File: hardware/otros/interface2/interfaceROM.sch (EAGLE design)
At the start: 15 parts, among them IC1 74HC174N, IC2 74HC32N, IC4 AM29F040S

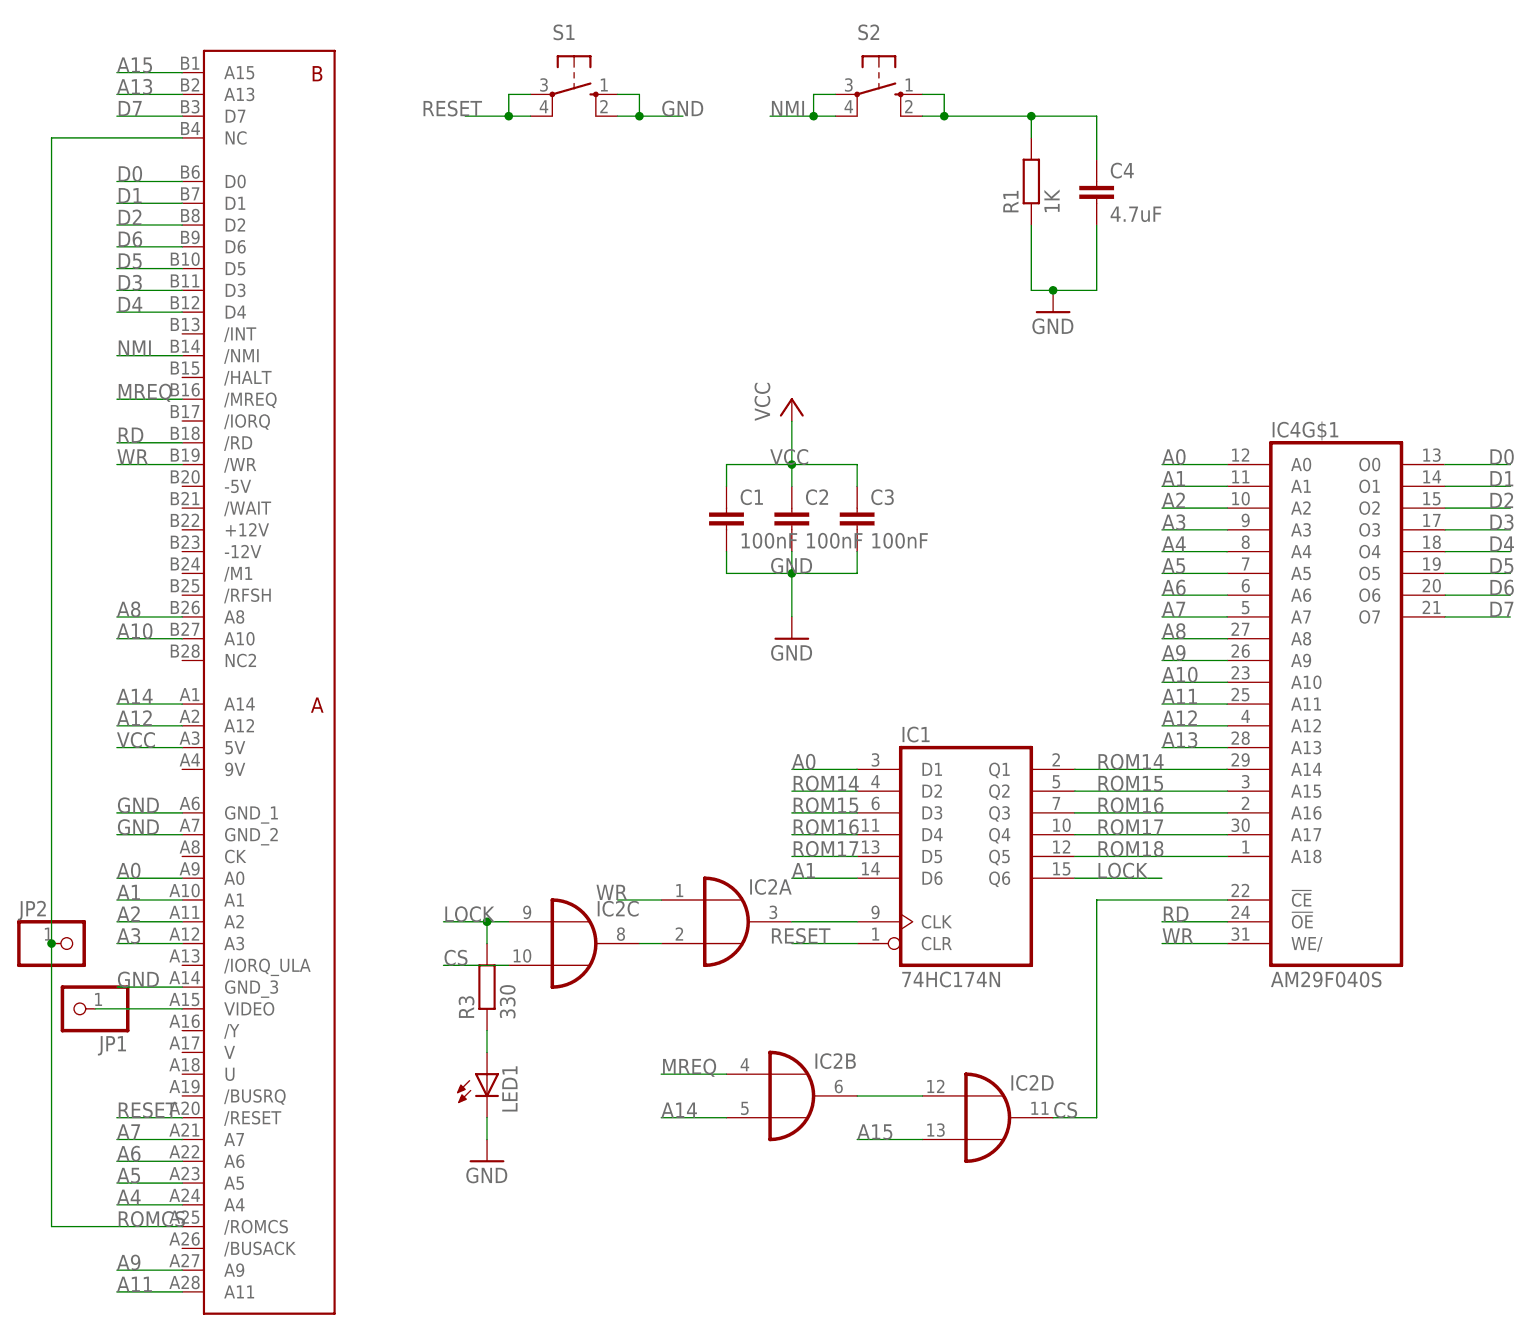
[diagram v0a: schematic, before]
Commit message: 
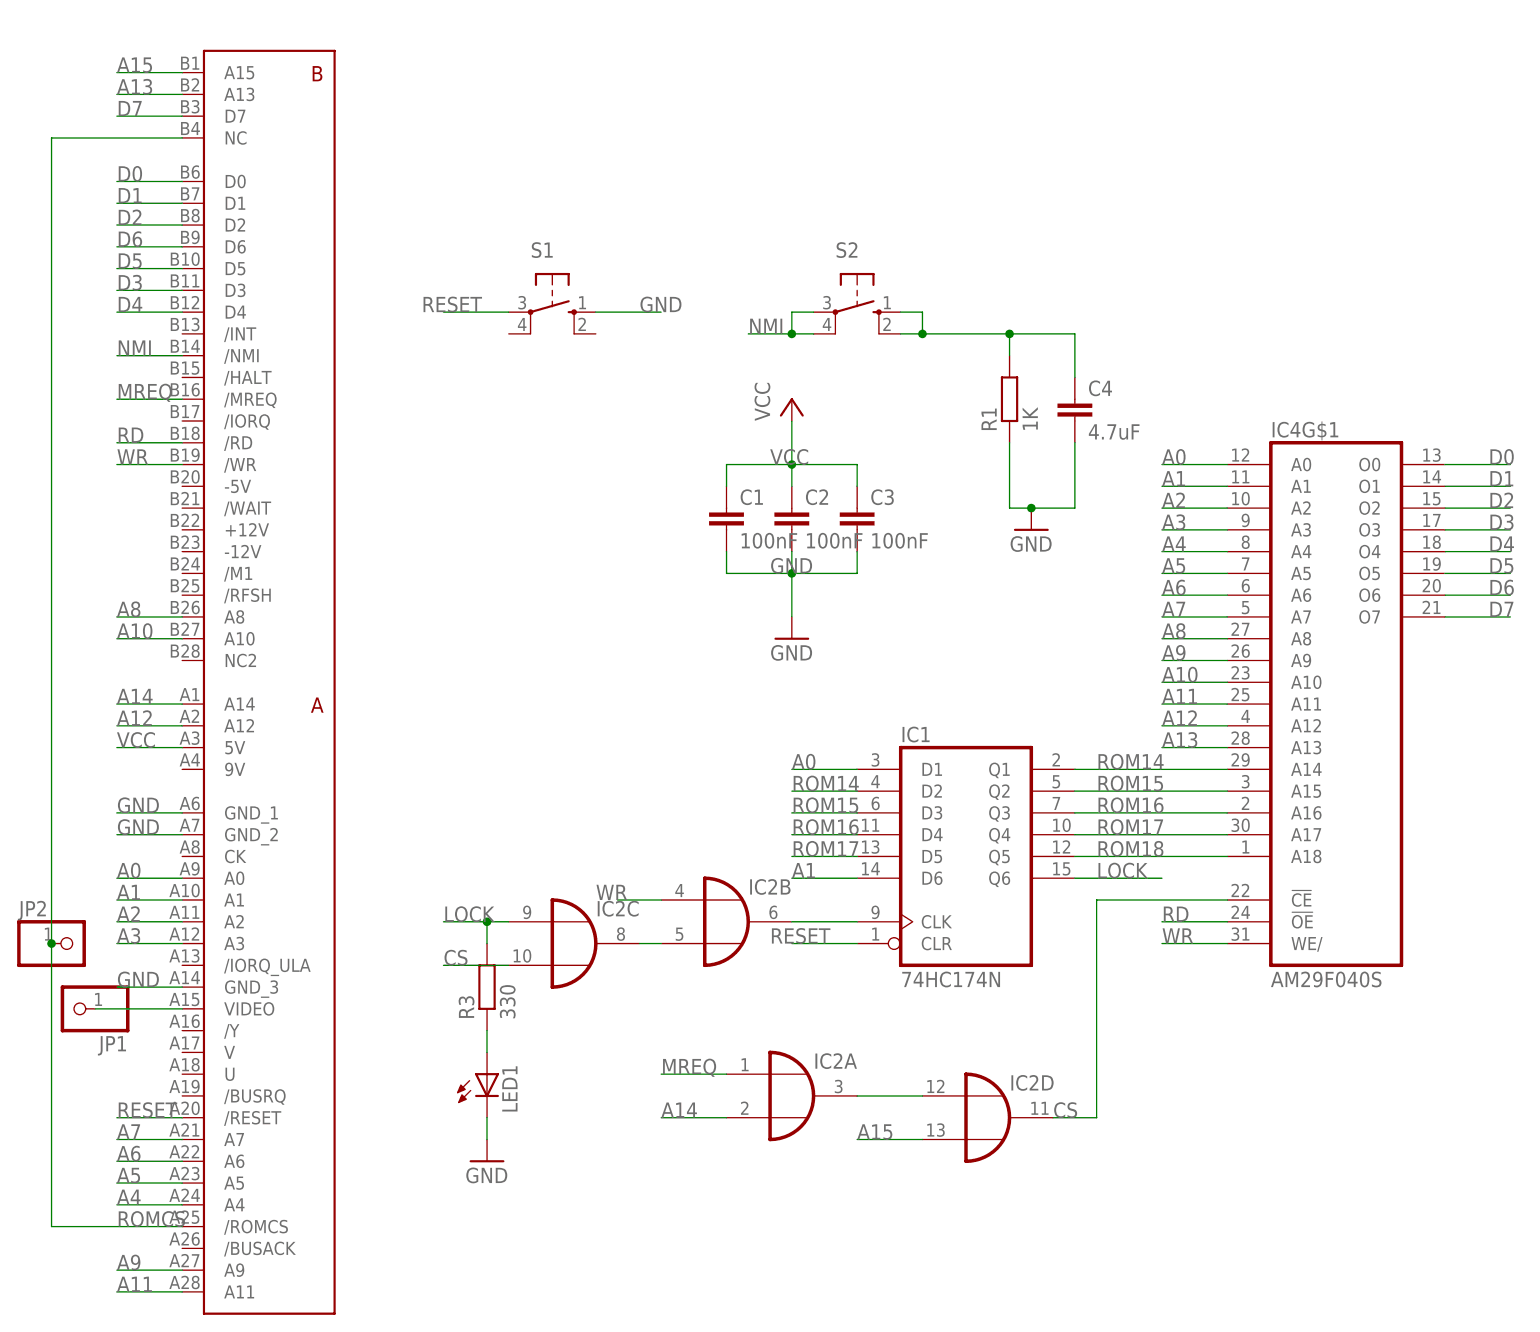
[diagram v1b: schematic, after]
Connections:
- net A14: now also IC2A.I1; no longer IC2B.I1
- net GND: no longer S1.S1
- net MREQ: now also IC2A.I0; no longer IC2B.I0
- net N$2: now also IC2B.O; no longer IC2A.O
- net N$3: now also IC2A.O; no longer IC2B.O
- net N$4: now also IC2B.I1; no longer IC2A.I1
- net RESET: no longer S1.P1
- net WR: now also IC2B.I0; no longer IC2A.I0
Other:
- moved on the sheet: C4, IC2A, IC2B, R1, S1, S2
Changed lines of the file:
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@@
 </plain>
 <instances>
-<instance part="S1" gate="1" x="48.26" y="78.74" rot="R270"/>
-<instance part="S2" gate="1" x="83.82" y="78.74" rot="R270"/>
+<instance part="S1" gate="1" x="45.72" y="53.34" rot="R270"/>
+<instance part="S2" gate="1" x="81.28" y="53.34" rot="R270"/>
 <instance part="U$3" gate="G$1" x="5.08" y="-63.5"/>
-<instance part="R1" gate="G$1" x="101.6" y="68.58" rot="R90"/>
-<instance part="C4" gate="G$1" x="109.22" y="68.58"/>
-<instance part="GND1" gate="1" x="104.14" y="53.34"/>
+<instance part="R1" gate="G$1" x="99.06" y="43.18" rot="R90"/>
+<instance part="C4" gate="G$1" x="106.68" y="43.18"/>
+<instance part="GND1" gate="1" x="101.6" y="27.94"/>
 <instance part="JP2" gate="G$1" x="-10.16" y="-20.32"/>
 <instance part="JP1" gate="G$1" x="-10.16" y="-27.94" rot="R180"/>
@@
 <instance part="C2" gate="G$1" x="73.66" y="30.48"/>
 <instance part="IC2" gate="C" x="48.26" y="-20.32"/>
-<instance part="IC2" gate="A" x="66.04" y="-17.78"/>
-<instance part="IC2" gate="B" x="73.66" y="-38.1"/>
+<instance part="IC2" gate="B" x="66.04" y="-17.78"/>
+<instance part="IC2" gate="A" x="73.66" y="-38.1"/>
 <instance part="IC2" gate="D" x="96.52" y="-40.64"/>
 </instances>
@@
 <segment>
 <pinref part="S2" gate="1" pin="S1"/>
-<wire x1="88.9" y1="76.2" x2="91.44" y2="76.2" width="0.1524" layer="91"/>
+<wire x1="86.36" y1="50.8" x2="88.9" y2="50.8" width="0.1524" layer="91"/>
 <pinref part="S2" gate="1" pin="S"/>
-<wire x1="88.9" y1="78.74" x2="91.44" y2="78.74" width="0.1524" layer="91"/>
-<wire x1="91.44" y1="78.74" x2="91.44" y2="76.2" width="0.1524" layer="91"/>
-<junction x="91.44" y="76.2"/>
+<wire x1="86.36" y1="53.34" x2="88.9" y2="53.34" width="0.1524" layer="91"/>
+<wire x1="88.9" y1="53.34" x2="88.9" y2="50.8" width="0.1524" layer="91"/>
+<junction x="88.9" y="50.8"/>
 <pinref part="C4" gate="G$1" pin="1"/>
-<wire x1="91.44" y1="76.2" x2="101.6" y2="76.2" width="0.1524" layer="91"/>
-<wire x1="101.6" y1="76.2" x2="109.22" y2="76.2" width="0.1524" layer="91"/>
-<wire x1="109.22" y1="76.2" x2="109.22" y2="71.12" width="0.1524" layer="91"/>
+<wire x1="88.9" y1="50.8" x2="99.06" y2="50.8" width="0.1524" layer="91"/>
+<wire x1="99.06" y1="50.8" x2="106.68" y2="50.8" width="0.1524" layer="91"/>
+<wire x1="106.68" y1="50.8" x2="106.68" y2="45.72" width="0.1524" layer="91"/>
 <pinref part="R1" gate="G$1" pin="2"/>
-<wire x1="101.6" y1="73.66" x2="101.6" y2="76.2" width="0.1524" layer="91"/>
-<junction x="101.6" y="76.2"/>
+<wire x1="99.06" y1="48.26" x2="99.06" y2="50.8" width="0.1524" layer="91"/>
+<junction x="99.06" y="50.8"/>
 </segment>
 </net>
@@
 <wire x1="58.42" y1="-40.64" x2="66.04" y2="-40.64" width="0.1524" layer="91"/>
 <label x="58.42" y="-40.64" size="1.778" layer="95"/>
-<pinref part="IC2" gate="B" pin="I1"/>
+<pinref part="IC2" gate="A" pin="I1"/>
 </segment>
 </net>
@@
 <wire x1="58.42" y1="-35.56" x2="66.04" y2="-35.56" width="0.1524" layer="91"/>
 <label x="58.42" y="-35.56" size="1.778" layer="95"/>
-<pinref part="IC2" gate="B" pin="I0"/>
+<pinref part="IC2" gate="A" pin="I0"/>
 </segment>
 </net>
@@
 <segment>
 <pinref part="S1" gate="1" pin="S"/>
-<wire x1="53.34" y1="78.74" x2="55.88" y2="78.74" width="0.1524" layer="91"/>
-<wire x1="55.88" y1="78.74" x2="55.88" y2="76.2" width="0.1524" layer="91"/>
-<pinref part="S1" gate="1" pin="S1"/>
-<wire x1="53.34" y1="76.2" x2="55.88" y2="76.2" width="0.1524" layer="91"/>
-<wire x1="60.96" y1="76.2" x2="55.88" y2="76.2" width="0.1524" layer="91"/>
-<junction x="55.88" y="76.2"/>
-<label x="58.42" y="76.2" size="1.778" layer="95"/>
+<wire x1="58.42" y1="53.34" x2="50.8" y2="53.34" width="0.1524" layer="91"/>
+<label x="55.88" y="53.34" size="1.778" layer="95"/>
 </segment>
 <segment>
 <pinref part="R1" gate="G$1" pin="1"/>
-<wire x1="101.6" y1="63.5" x2="101.6" y2="55.88" width="0.1524" layer="91"/>
+<wire x1="99.06" y1="38.1" x2="99.06" y2="30.48" width="0.1524" layer="91"/>
 <pinref part="C4" gate="G$1" pin="2"/>
-<wire x1="101.6" y1="55.88" x2="104.14" y2="55.88" width="0.1524" layer="91"/>
-<wire x1="104.14" y1="55.88" x2="109.22" y2="55.88" width="0.1524" layer="91"/>
-<wire x1="109.22" y1="55.88" x2="109.22" y2="63.5" width="0.1524" layer="91"/>
+<wire x1="99.06" y1="30.48" x2="101.6" y2="30.48" width="0.1524" layer="91"/>
+<wire x1="101.6" y1="30.48" x2="106.68" y2="30.48" width="0.1524" layer="91"/>
+<wire x1="106.68" y1="30.48" x2="106.68" y2="38.1" width="0.1524" layer="91"/>
 <pinref part="GND1" gate="1" pin="GND"/>
-<junction x="104.14" y="55.88"/>
+<junction x="101.6" y="30.48"/>
 </segment>
 <segment>
@@
 <segment>
 <pinref part="S2" gate="1" pin="P1"/>
-<wire x1="71.12" y1="76.2" x2="76.2" y2="76.2" width="0.1524" layer="91"/>
+<wire x1="68.58" y1="50.8" x2="73.66" y2="50.8" width="0.1524" layer="91"/>
 <pinref part="S2" gate="1" pin="P"/>
-<wire x1="76.2" y1="76.2" x2="78.74" y2="76.2" width="0.1524" layer="91"/>
-<wire x1="78.74" y1="78.74" x2="76.2" y2="78.74" width="0.1524" layer="91"/>
-<wire x1="76.2" y1="78.74" x2="76.2" y2="76.2" width="0.1524" layer="91"/>
-<junction x="76.2" y="76.2"/>
-<label x="71.12" y="76.2" size="1.778" layer="95"/>
+<wire x1="73.66" y1="50.8" x2="76.2" y2="50.8" width="0.1524" layer="91"/>
+<wire x1="76.2" y1="53.34" x2="73.66" y2="53.34" width="0.1524" layer="91"/>
+<wire x1="73.66" y1="53.34" x2="73.66" y2="50.8" width="0.1524" layer="91"/>
+<junction x="73.66" y="50.8"/>
+<label x="68.58" y="50.8" size="1.778" layer="95"/>
 </segment>
 </net>
@@
 <segment>
 <pinref part="S1" gate="1" pin="P"/>
-<wire x1="43.18" y1="78.74" x2="40.64" y2="78.74" width="0.1524" layer="91"/>
-<wire x1="40.64" y1="78.74" x2="40.64" y2="76.2" width="0.1524" layer="91"/>
-<wire x1="40.64" y1="76.2" x2="35.56" y2="76.2" width="0.1524" layer="91"/>
-<pinref part="S1" gate="1" pin="P1"/>
-<wire x1="43.18" y1="76.2" x2="40.64" y2="76.2" width="0.1524" layer="91"/>
-<junction x="40.64" y="76.2"/>
-<label x="30.48" y="76.2" size="1.778" layer="95"/>
+<wire x1="40.64" y1="53.34" x2="33.02" y2="53.34" width="0.1524" layer="91"/>
+<label x="30.48" y="53.34" size="1.778" layer="95"/>
 </segment>
 <segment>
@@
 </segment>
 <segment>
-<pinref part="IC2" gate="A" pin="I0"/>
+<pinref part="IC2" gate="B" pin="I0"/>
 <wire x1="58.42" y1="-15.24" x2="53.34" y2="-15.24" width="0.1524" layer="91"/>
 <label x="50.8" y="-15.24" size="1.778" layer="95"/>
@@
 <wire x1="73.66" y1="-17.78" x2="81.28" y2="-17.78" width="0.1524" layer="91"/>
 <pinref part="IC1" gate="A" pin="CLK"/>
-<pinref part="IC2" gate="A" pin="O"/>
+<pinref part="IC2" gate="B" pin="O"/>
 </segment>
 </net>
@@
 <net name="N$3" class="0">
 <segment>
-<pinref part="IC2" gate="B" pin="O"/>
+<pinref part="IC2" gate="A" pin="O"/>
 <pinref part="IC2" gate="D" pin="I0"/>
 <wire x1="88.9" y1="-38.1" x2="81.28" y2="-38.1" width="0.1524" layer="91"/>
@@
 <net name="N$4" class="0">
 <segment>
-<pinref part="IC2" gate="A" pin="I1"/>
+<pinref part="IC2" gate="B" pin="I1"/>
 <pinref part="IC2" gate="C" pin="O"/>
 <wire x1="58.42" y1="-20.32" x2="55.88" y2="-20.32" width="0.1524" layer="91"/>

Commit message: 
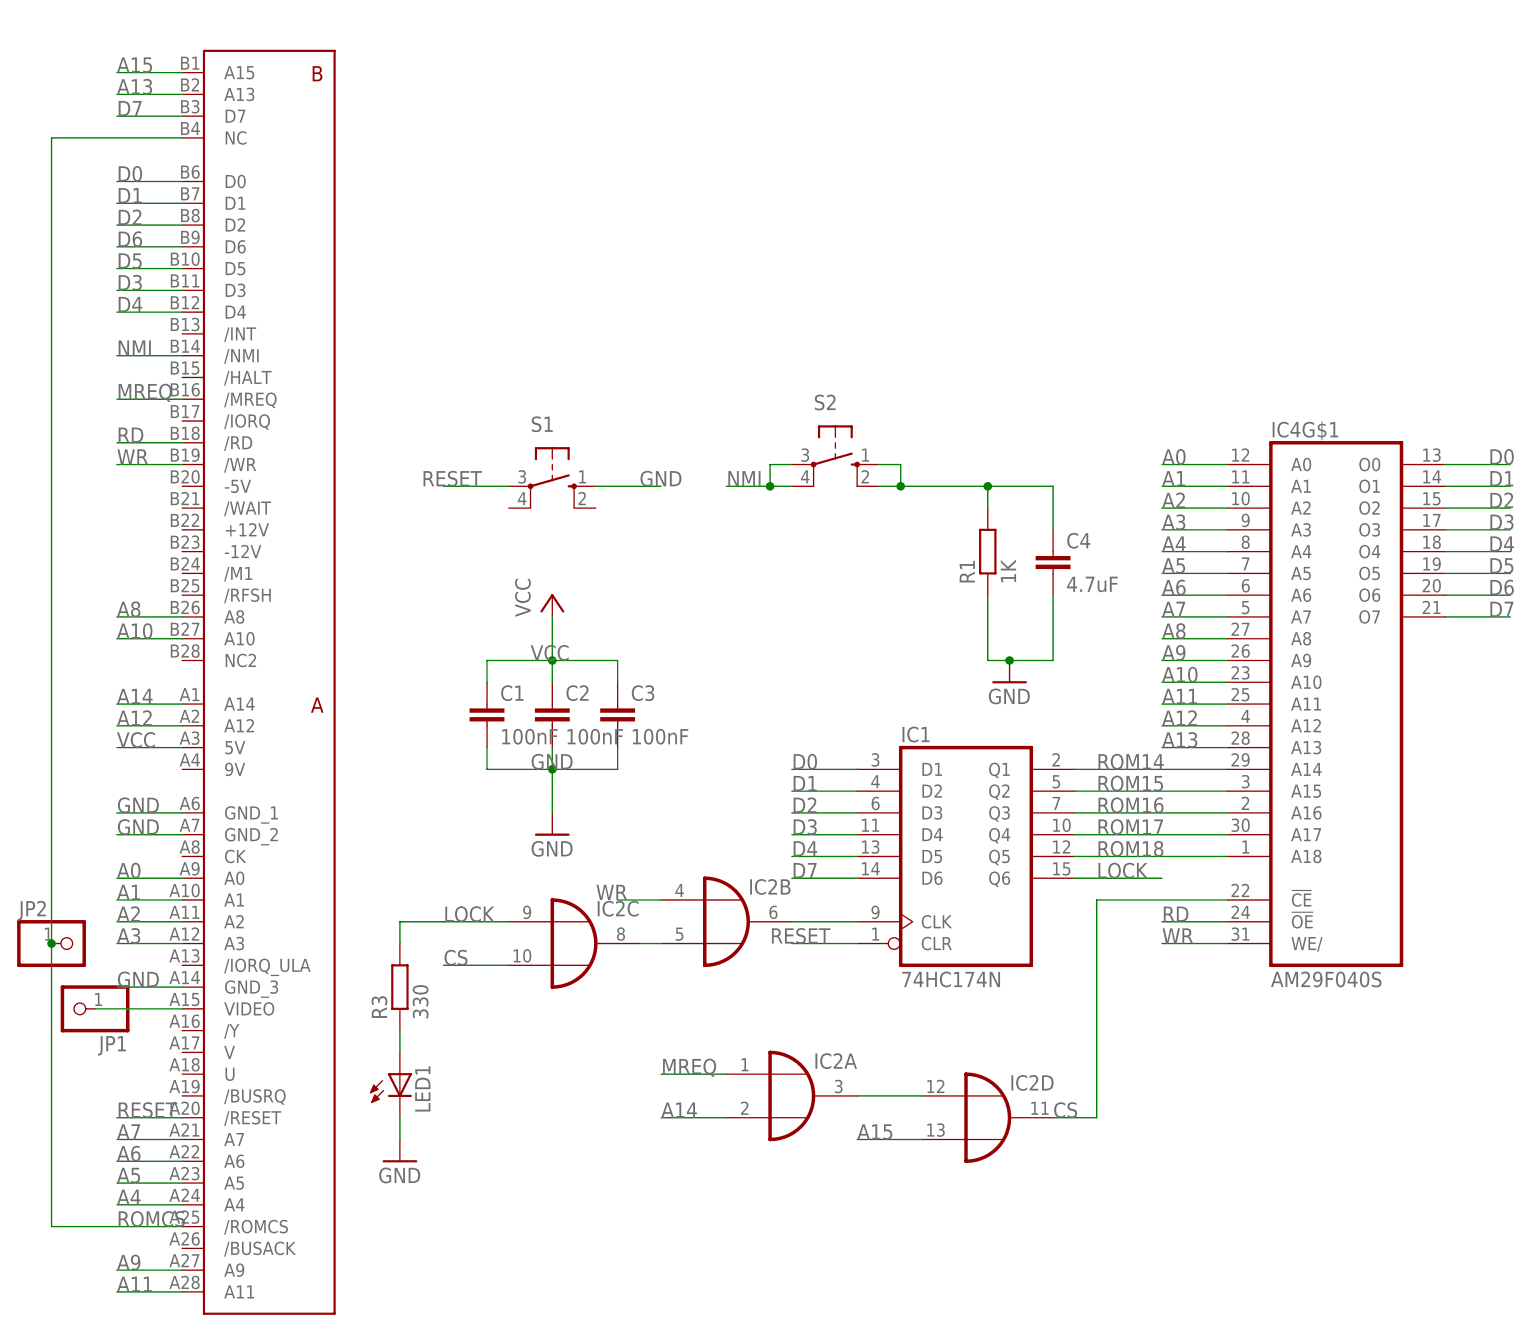
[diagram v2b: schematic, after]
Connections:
- net A0: no longer IC1A.D1
- net A1: no longer IC1A.D6
- net D0: now also IC1A.D1
- net D1: now also IC1A.D2
- net D2: now also IC1A.D3
- net D3: now also IC1A.D4
- net D4: now also IC1A.D5
- net D7: now also IC1A.D6
- net ROM14: no longer IC1A.D2
- net ROM15: no longer IC1A.D3
- net ROM16: no longer IC1A.D4
- net ROM17: no longer IC1A.D5
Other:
- moved on the sheet: C1, C2, C3, C4, LED1, R1, R3, S1, S2

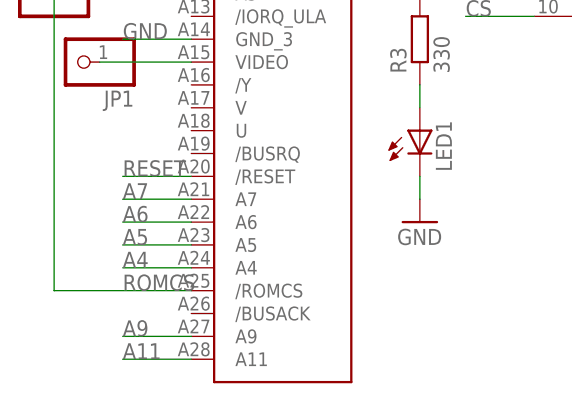
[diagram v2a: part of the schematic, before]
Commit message: Fix de la placa interface ROM, había que conectar ROMCS a VCC
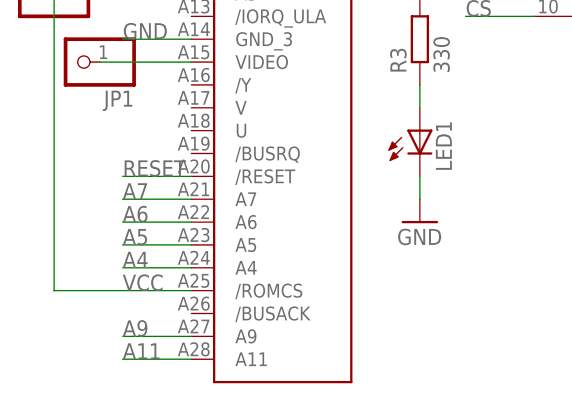
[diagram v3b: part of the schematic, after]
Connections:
- removed net ROMCS: JP2.1, U$3./ROMCS, U$3.NC
- net VCC: now also JP2.1, U$3./ROMCS, U$3.NC
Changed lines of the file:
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@@
-</segment>
-</net>
-<net name="ROMCS" class="0">
-<segment>
-<pinref part="U$3" gate="G$1" pin="/ROMCS"/>
-<label x="-5.08" y="-53.34" size="1.778" layer="95"/>
-<pinref part="U$3" gate="G$1" pin="NC"/>
-<wire x1="2.54" y1="73.66" x2="-12.7" y2="73.66" width="0.1524" layer="91"/>
-<wire x1="-12.7" y1="-53.34" x2="-12.7" y2="-20.32" width="0.1524" layer="91"/>
-<wire x1="-12.7" y1="-20.32" x2="-12.7" y2="73.66" width="0.1524" layer="91"/>
-<wire x1="-12.7" y1="-53.34" x2="2.54" y2="-53.34" width="0.1524" layer="91"/>
-<pinref part="JP2" gate="G$1" pin="1"/>
-<junction x="-12.7" y="-20.32"/>
 </segment>
 </net>
@@
 <wire x1="38.1" y1="12.7" x2="45.72" y2="12.7" width="0.1524" layer="91"/>
 </segment>
-</net>
+<segment>
+<pinref part="U$3" gate="G$1" pin="/ROMCS"/>
+<label x="-5.08" y="-53.34" size="1.778" layer="95"/>
+<pinref part="U$3" gate="G$1" pin="NC"/>
+<wire x1="2.54" y1="73.66" x2="-12.7" y2="73.66" width="0.1524" layer="91"/>
+<wire x1="-12.7" y1="-53.34" x2="-12.7" y2="-20.32" width="0.1524" layer="91"/>
+<wire x1="-12.7" y1="-20.32" x2="-12.7" y2="73.66" width="0.1524" layer="91"/>
+<wire x1="-12.7" y1="-53.34" x2="2.54" y2="-53.34" width="0.1524" layer="91"/>
+<pinref part="JP2" gate="G$1" pin="1"/>
+<junction x="-12.7" y="-20.32"/>
+</segment>
+</net>
